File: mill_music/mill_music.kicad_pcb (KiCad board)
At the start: 2 copper layers, 82.8 x 51.3 mm, 50 parts, among them J1 Conn_02x03_Odd_Even, J2 Screw_Terminal_01x02, J3 Screw_Terminal_01x02, J4 Screw_Terminal_01x02, SW1 SW_Push, SW2 SW_Push, SW3 SW_Push, SW4 SW_Push, SW5 SW_Push, SW6 SW_Push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

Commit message: Mill Music: add copyright and PDF
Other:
- board text added: "https://github.com/jonronen/kicad-stuff/ Mill Music (c) 2021"
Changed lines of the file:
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@@
   (general
     (thickness 1.6)
-    (drawings 5)
+    (drawings 6)
     (tracks 252)
     (zones 0)
@@
     )
   )
+  (gr_text "https://github.com/jonronen/kicad-stuff/\nMill Music\n(c) 2021" (at 134.112 117.094) (layer B.SilkS)
+    (effects (font (size 1 1) (thickness 0.15)) (justify mirror))
+  )
   (gr_circle (center 181.864 114.554) (end 182.118 114.046) (layer F.SilkS) (width 0.12))

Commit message: Mill Music: add more text on the board
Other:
- board text added: "+12V"
- board text added: "0"
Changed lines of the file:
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@@
   (general
     (thickness 1.6)
-    (drawings 6)
+    (drawings 9)
     (tracks 252)
     (zones 0)
@@
     )
   )
+  (gr_text 0 (at 122.682 90.17) (layer F.SilkS)
+    (effects (font (size 1 1) (thickness 0.15)))
+  )
+  (gr_text +12V (at 136.906 90.424) (layer F.SilkS)
+    (effects (font (size 1 1) (thickness 0.15)))
+  )
+  (gr_circle (center 171.958 97.536) (end 172.212 97.028) (layer F.SilkS) (width 0.12))
   (gr_text "https://github.com/jonronen/kicad-stuff/\nMill Music\n(c) 2021" (at 134.112 117.094) (layer B.SilkS)
     (effects (font (size 1 1) (thickness 0.15)) (justify mirror))

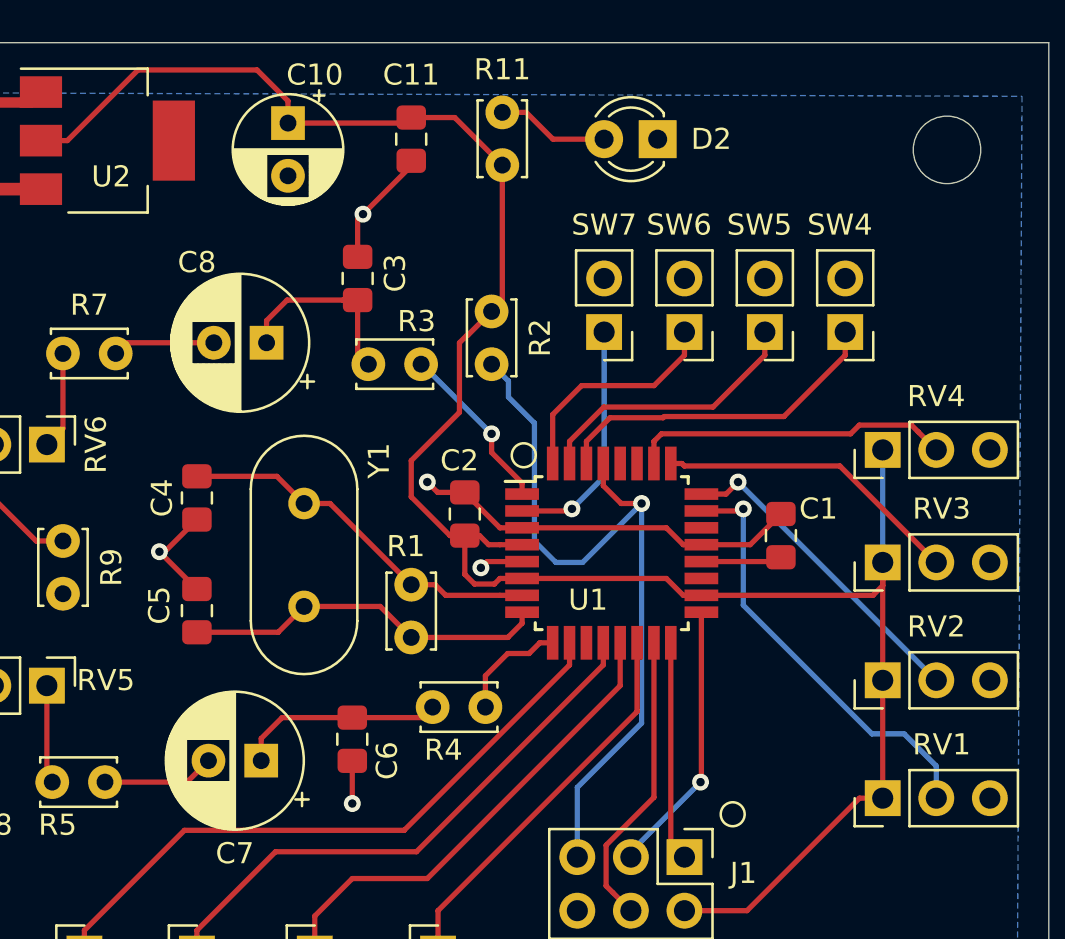
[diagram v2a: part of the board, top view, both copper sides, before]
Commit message: Mill Music: update footprints and PCB
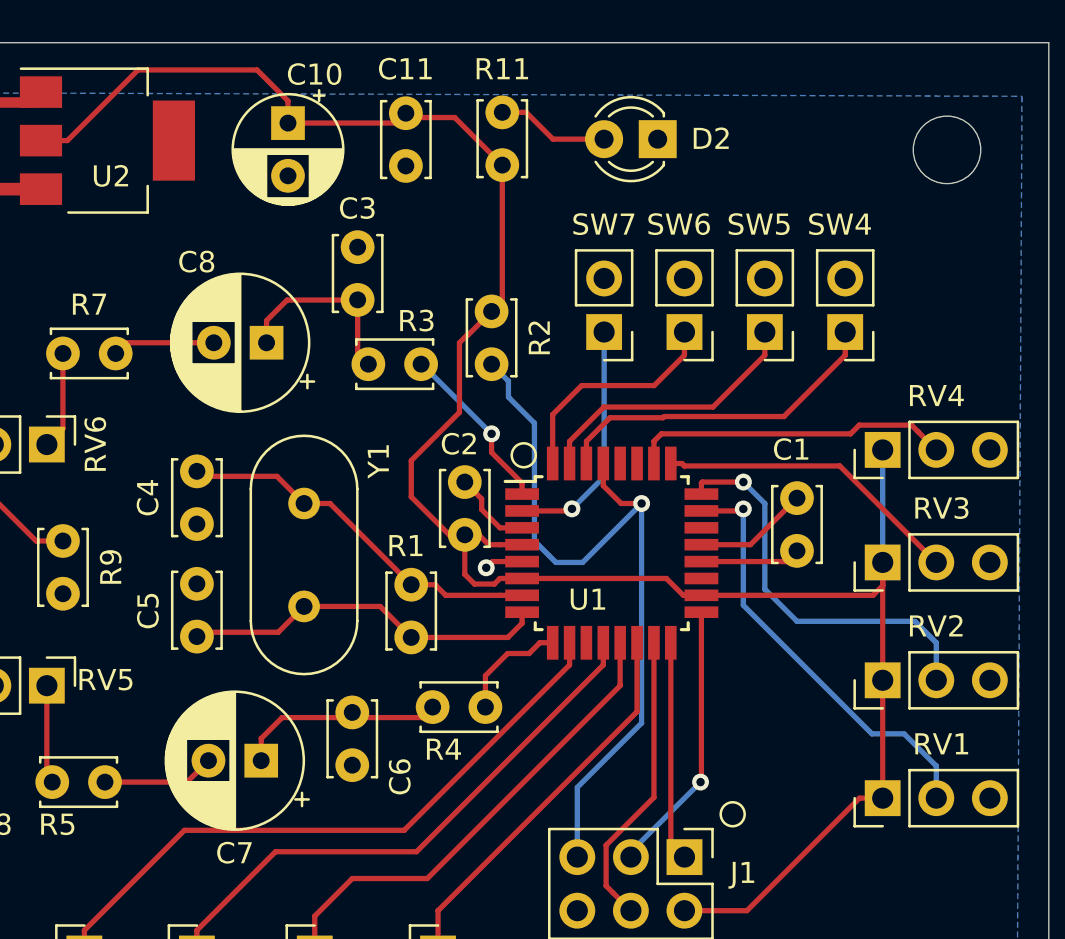
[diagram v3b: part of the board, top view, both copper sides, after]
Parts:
- C1, C11, C2, C3, C4, C5, C6: footprint Capacitor_SMD:C_0805_2012Metric_Pad1.15x1.40mm_HandSolder -> Capacitor_THT:C_Disc_D3.4mm_W2.1mm_P2.50mm
- moved C11 1.30 mm to (166.4, 83.8)
- moved C6 1.27 mm to (163.8, 109.7)
- moved C5 1.27 mm to (156.5, 103.6)
- moved C4 1.24 mm to (156.5, 100.8)
- moved C1 1.05 mm to (184.9, 102.1)
- moved C3 1.02 mm to (164.1, 90.2)
- moved C2 0.98 mm to (169.2, 101.3)
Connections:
- U1 pad 11: (no net) -> Net-(U1-Pad11)
- U1 pad 19: (no net) -> Net-(U1-Pad19)
- U1 pad 22: (no net) -> Net-(U1-Pad22)
- U1 pad 27: (no net) -> Net-(U1-Pad27)
- U1 pad 28: (no net) -> Net-(U1-Pad28)
- U3 pad 10: (no net) -> Net-(U3-Pad10)
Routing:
- net GND: track 38.7 -> 16.7 mm, vias 5 -> 1
- net /ADC1: track 15.3 -> 19.0 mm
- net Net-(C1-Pad1): track 3.85 -> 4.74 mm

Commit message: New music platform revision
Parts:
- added RV10: 47K, Connector_PinHeader_2.54mm:PinHeader_1x03_P2.54mm_Vertical, F.Cu at (187.5, 110.7)
- added RV7: 47K, Connector_PinHeader_2.54mm:PinHeader_1x03_P2.54mm_Vertical, F.Cu at (192.5, 93.7)
- added RV8: 47K, Connector_PinHeader_2.54mm:PinHeader_1x03_P2.54mm_Vertical, F.Cu at (192.5, 88.4)
- added RV9: 47K, Connector_PinHeader_2.54mm:PinHeader_1x03_P2.54mm_Vertical, F.Cu at (182.1, 110.7)
- added SW9: SW_Push, Connector_PinHeader_2.54mm:PinHeader_1x02_P2.54mm_Vertical, F.Cu at (172.0, 119.4)
- moved RV2 9.49 mm to (198.1, 110.7), turned to 0 degrees
- moved J1 6.31 mm to (183.6, 121.4)
- moved RV1 4.88 mm to (192.8, 110.7), turned to 0 degrees
- moved H2 4.83 mm to (196.3, 123.2)
- moved H1 4.33 mm to (196.3, 82.8)
- moved RV3 4.10 mm to (192.5, 104.6)
- moved RV4 4.10 mm to (192.5, 99.3)
- moved SW3 2.34 mm to (166.4, 119.4)
- moved SW1 2.18 mm to (155.2, 119.4)
- moved SW2 2.18 mm to (160.8, 119.4)
- moved SW8 2.18 mm to (149.9, 119.4)
- moved H4 0.72 mm to (117.6, 82.8)
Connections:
- U1 pad 11: Net-(U1-Pad11) -> /BTN9
- U1 pad 19: Net-(U1-Pad19) -> /ADC6
- U1 pad 22: Net-(U1-Pad22) -> /ADC7
- U1 pad 27: Net-(U1-Pad27) -> /ADC4
- U1 pad 28: Net-(U1-Pad28) -> /ADC5
- U3 pad 10: Net-(U3-Pad10) -> (no net)
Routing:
- net +5V: track 101.4 -> 143.6 mm
- net /ADC5: track 0.00 -> 23.0 mm
- net /ADC7: track 0.00 -> 21.8 mm
- net /ADC4: track 0.00 -> 20.1 mm
- net /BTN9: track 0.00 -> 14.4 mm, vias 0 -> 1
- net /ADC6: track 0.00 -> 13.1 mm
- net Net-(J1-Pad4): track 14.1 -> 22.9 mm
- net /ADC1: track 19.0 -> 27.0 mm, vias 1 -> 0
- net Net-(J1-Pad1): track 10.4 -> 16.9 mm, vias 0 -> 1
- net Net-(J1-Pad5): track 37.1 -> 43.4 mm
- net Net-(J1-Pad3): track 13.0 -> 18.5 mm, vias 1 -> 0
- net /ADC2: track 14.5 -> 19.6 mm
- net /ADC0: track 20.4 -> 24.4 mm, vias 1 -> 0
- net /ADC3: track 15.2 -> 19.2 mm
- net /BTN1: track 26.6 -> 28.2 mm
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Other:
- board size 82.8 x 51.3 mm -> 87.1 x 51.3 mm
